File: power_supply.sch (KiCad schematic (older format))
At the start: 29 parts, among them J5 USB_A_stacked, U3 AP22802A, U4 IP4220CZ6, U5 AP2210-3.3, U8 TPS2513, U9 AP6502

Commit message: Several improvements (v0.4) after first tests
- Ultra-low-power MCU STM32L072
- Larger screw terminals
- USB power supply replaced by more efficient SMPS
- High-side load switch with P-MOS
- High-side current measurement to include USB current in load measurement
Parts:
- removed C41: 100n, LibreSolar:C_0603_1608, symbol Project:C
- removed D2: SS14FL, LibreSolar:D_SOD-123, symbol Project:D_Schottky
- removed R33, R34: 0R, LibreSolar:R_0603_1608, symbol Project:R
- removed R35: 6.8k, LibreSolar:R_0603_1608, symbol Project:R
- removed R50: 100k, LibreSolar:R_0603_1608, symbol Project:R
- removed U3: AP22802A, Package_TO_SOT_SMD:SOT-23-5, symbol Project:AP22802A
- added C2: 150u, Capacitor_SMD:CP_Elec_8x6.2, symbol Project:CP
- added C22: 2.2u, LibreSolar:C_0603_1608, symbol Project:C
- added C40: 22u, LibreSolar:C_1206_3216, symbol Project:C
- added D7: 1N4148, LibreSolar:D_SOD-123, symbol Project:D
- added D8: 11V, LibreSolar:D_SOD-123, symbol Project:D_Zener
- added J7: PWR_5V, Connector_PinHeader_2.54mm:PinHeader_1x02_P2.54mm_Vertical, symbol Connector:Conn_01x02_Male
- added Q5: BSS138N, LibreSolar:SOT-23, symbol Device:Q_NMOS_GSD
- added Q6: DMP3099L-7, LibreSolar:SOT-23, symbol Device:Q_PMOS_GSD
- added R12: 100k, LibreSolar:R_0603_1608, symbol Project:R
- added R31: 10k, LibreSolar:R_0603_1608, symbol Project:R
- added R32: 4.7, LibreSolar:R_0805_2012, symbol Project:R
- added TP7, TP8, TP9: Test_Point_Probe, TestPoint:TestPoint_Pad_D1.0mm, symbol Connector:TestPoint_Probe
- C15: value 22u -> 10u; footprint LibreSolar:C_0805_2012 -> LibreSolar:C_1210_3225; Manufacturer Murata -> Samsung; PartNumber GRM21BR61E226ME44L -> CL31A106KAHNNNE; Remarks 25V, X5R -> 25V, X7R
- C20, C21: value 47u -> 22u; footprint LibreSolar:C_0805_2012 -> LibreSolar:C_1206_3216; Manufacturer Murata -> Samsung; PartNumber GRM21BR61A476ME15K -> CL31B226MPHNNNE
- C24, U8: Config (none) -> +fastusb; DNF (none) -> X
- C29: value 1u -> 220n; footprint LibreSolar:C_0805_2012 -> LibreSolar:C_0603_1608; Manufacturer Yageo -> Murata; PartNumber CC0805KKX7R9BB105 -> GCM188R71E224KA55D; Remarks (none) -> 25V, X7R
- C36: value 6.8n -> 22u; footprint LibreSolar:C_0603_1608 -> LibreSolar:C_1206_3216; Manufacturer Yageo -> Samsung; PartNumber CC0603KRX7R9BB682 -> CL31B226MPHNNNE; Remarks (none) -> 10V
- L2: footprint Inductor_SMD:L_0805_2012Metric -> Inductor_SMD:L_1210_3225Metric; Manufacturer Murata -> Tayo Yuden; PartNumber DFE201210U-2R2M=P2 -> BRL3225T2R2M
- L3: footprint LibreSolar:Bourns_SRN6045TA -> LibreSolar:Bourns_SRN8040TA; Alternative Bourns SRN6045TA-100M -> Bourns SRN8040TA-100M; PartNumber NR6045T100M -> NR8040T100M
- R28: value 45.3k -> 100k; PartNumber RC0603FR-0745K3L -> RC0603FR-07100KL
- R29: value 10k -> 24.9k; PartNumber RC0603FR-0710KL -> RC0603FR-0724K9L
- U9: value AP6502 -> LMR33630; symbol Project:MP2307 -> LibreSolar:LMR33630; Alternatives MP2307DN-LF-Z -> (none); Manufacturer Diodes Inc. -> Texas Instruments; PartNumber AP6502ASP-13 -> LMR33630ADDA; Remarks (none) -> 400 kHz version
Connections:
- net +3V3: now also TP9.1
- net +5V: now also C24.1, C36.1, J5.1 (VBUS1), J5.5 (VBUS2), U4.5, U8.5 (IN), C40.1, D7.2 (A), J7.1 (Pin_1), TP7.1; no longer C23.1, C29.1, U5.1 (IN), U5.3 (EN)
- net GND: now also C36.2, U9.1 (PGND), C2.2, C22.2, C40.2, D8.2 (A), J7.2 (Pin_2); no longer U9.4 (GND)
- net USB_PWR_EN: now also U9.3 (EN)
- net at C19.2, L3.1: now also U9.8 (SW); no longer U9.3 (SW)
- net at C19.1: now also U9.7 (BOOT); no longer U9.1 (BS)
- net at C15.1, L2.2, U9.2 (VIN): now also C29.1, C2.1
- net at U9.6 (VCC): now also C26.1; no longer C36.1
- net +12V renamed LOAD_S
- new net: C23.1, D7.1 (K), Q6.3 (D), U5.1 (IN), U5.3 (EN)
- new net: D8.1 (K), Q5.1 (G), R31.1
- new net +10V: C22.1, Q5.2 (S), Q6.2 (S), R12.2, R32.2, TP8.1
- new net DCDC_OUT: Q5.3 (D), R31.2, R32.1
- new net PG_5V: Q6.1 (G), R12.1, U9.4 (PG)
- no-connect marks 0 -> 2
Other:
- note added: "Fast charging only on top USB port\nBottom USB port for data connection"
- note added: "Stuffing options for MOSFET\ndriver supply voltage:\n\n1. Direct supply via 12V (put R32)\n\n2. Source follower to generate\n10V from higher bat. voltage"
- note added: "Supply from 10V rail\nonly if 5V supply is \nnot good enough\n\n(maybe the gate\ncould be tied to\n5V for SMPS w/o PG)"
- note added: "Test results TP8 using 11V zener:\n- 9.28 V with MOSFET driver on \n (50 kHz)\n- 9.62 V with MOSFET driver off\n\n--> 12V zener might be better"
- note removed: "Alternative parts:\nMonolithic Power MP2307\nTI TPS5433x\nDiodes Inc. AP6502"
- moved on the sheet: C14, C15, C19, C20, C21, C23, C24, C25, C26, C35, C38, J5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

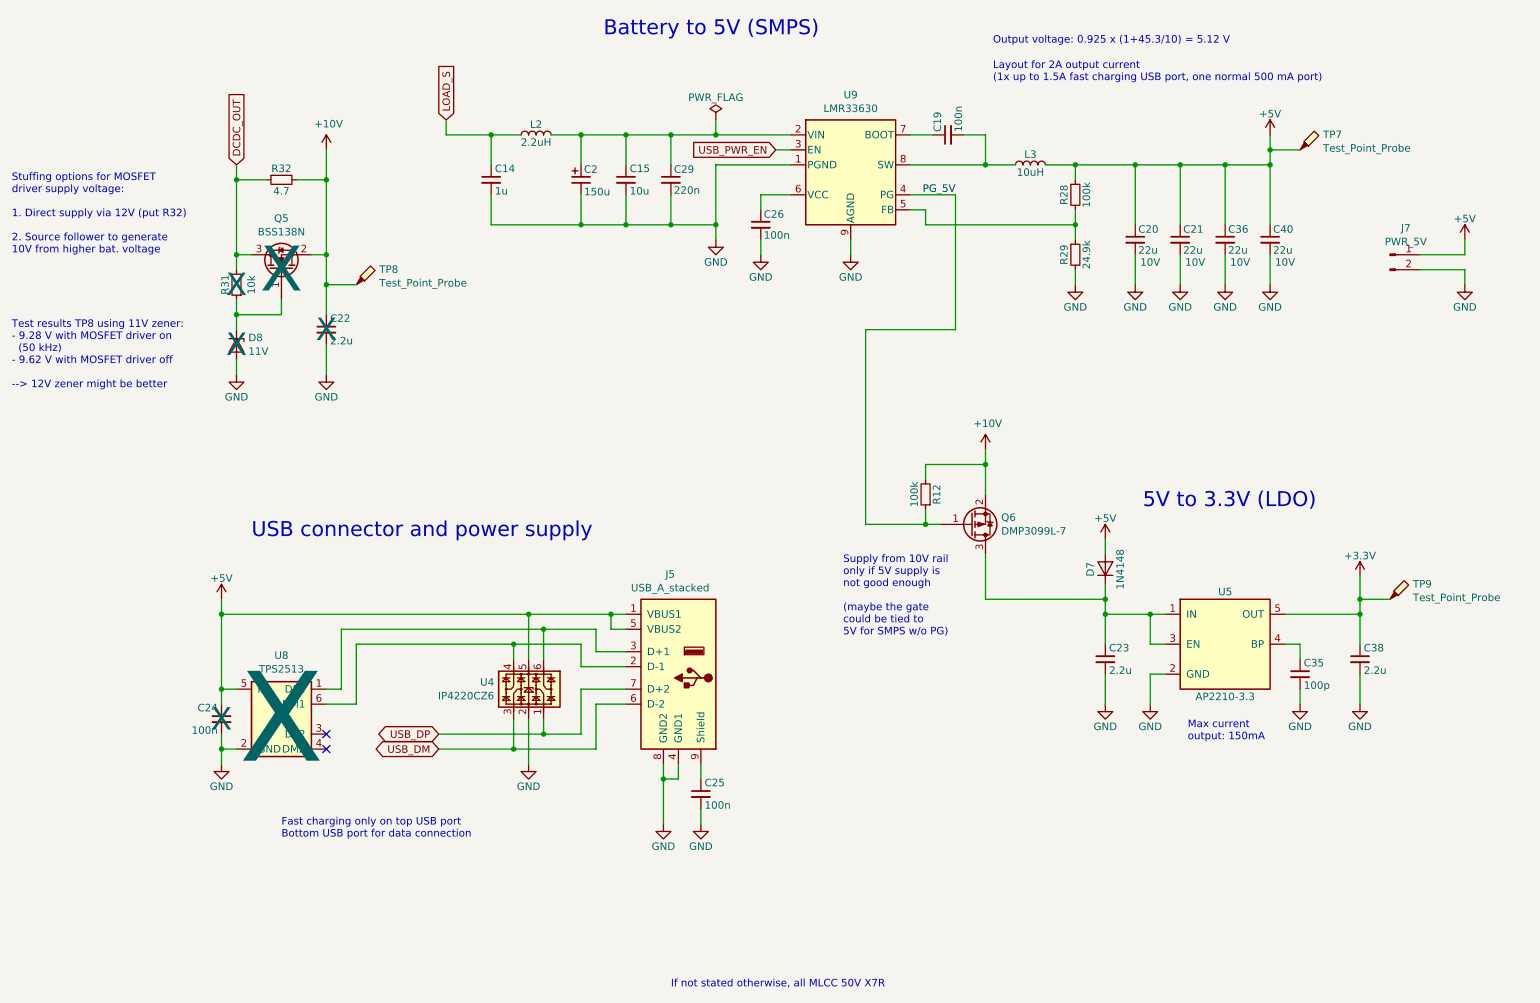
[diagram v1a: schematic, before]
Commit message: Board shape adjusted and 6P6C connector added
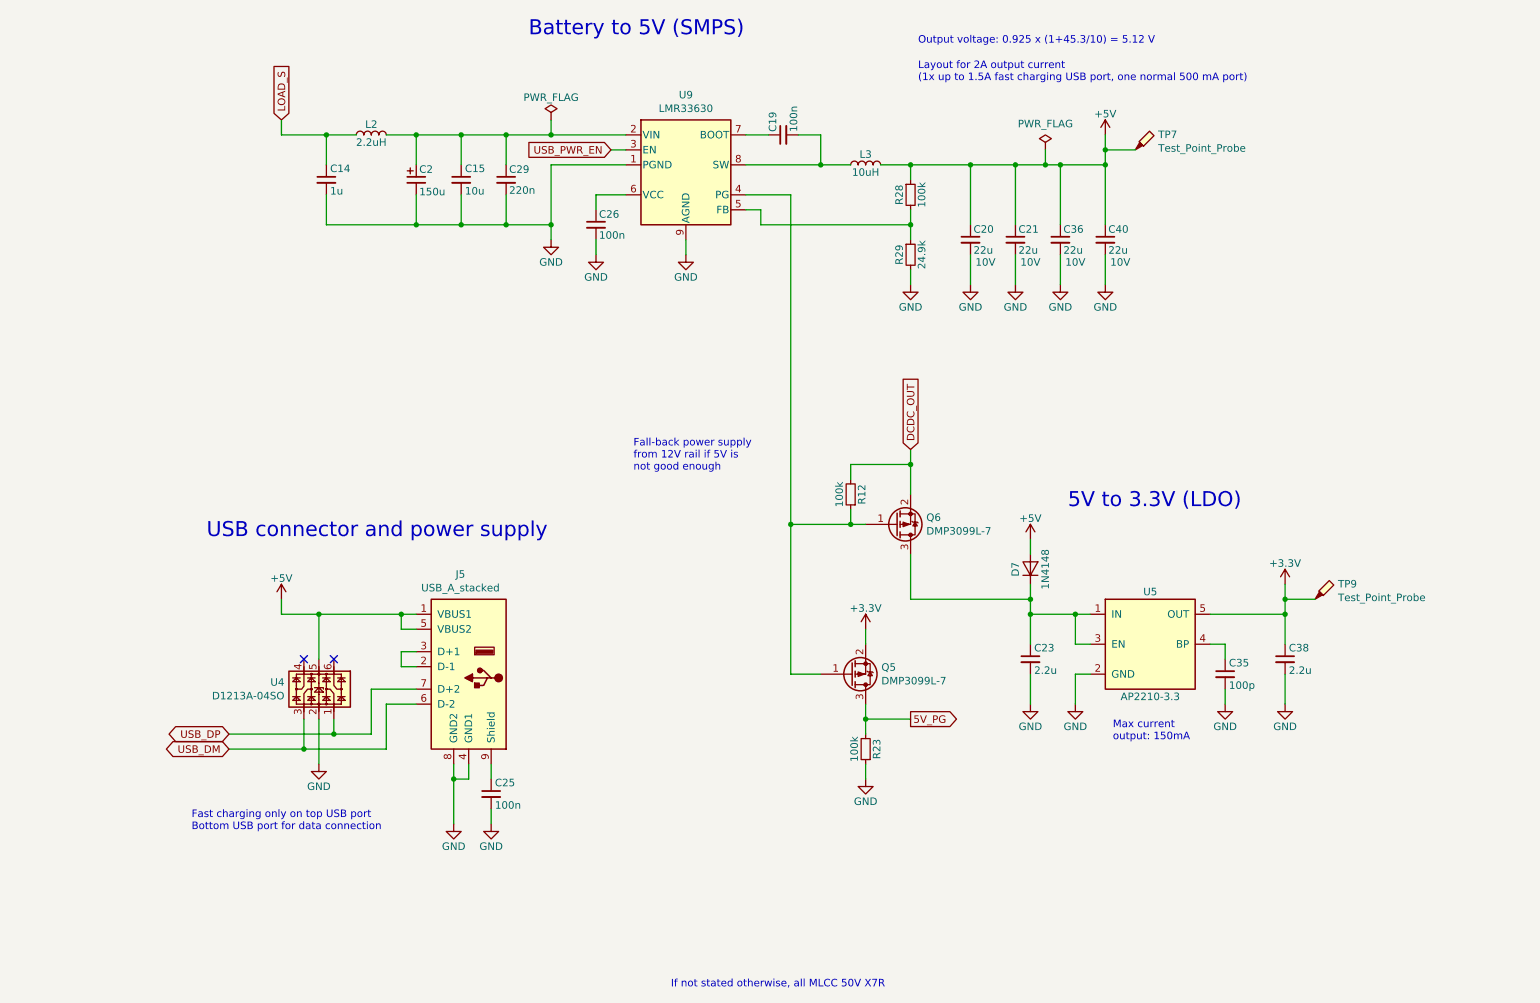
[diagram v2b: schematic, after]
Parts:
- removed C22: 2.2u, LibreSolar:C_0603_1608, symbol Project:C
- removed C24: 100n, LibreSolar:C_0603_1608, symbol Project:C
- removed D8: 11V, LibreSolar:D_SOD-123, symbol Project:D_Zener
- removed J7: PWR_5V, Connector_PinHeader_2.54mm:PinHeader_1x02_P2.54mm_Vertical, symbol Connector:Conn_01x02_Male
- removed Q5: BSS138N, LibreSolar:SOT-23, symbol Device:Q_NMOS_GSD
- removed R31: 10k, LibreSolar:R_0603_1608, symbol Project:R
- removed R32: 4.7, LibreSolar:R_0805_2012, symbol Project:R
- removed TP8: Test_Point_Probe, TestPoint:TestPoint_Pad_D1.0mm, symbol Connector:TestPoint_Probe
- removed U8: TPS2513, LibreSolar:SOT-23-6, symbol Interface_USB:TPS2513
- added Q5: DMP3099L-7, LibreSolar:SOT-23, symbol Device:Q_PMOS_GSD
- added R23: 100k, LibreSolar:R_0603_1608, symbol Project:R
- J5: Alternative Wuerth 61400826021 -> (none); Remarks (none) -> Alternative: Wuerth 61400826021
- L3: Alternative Bourns SRN8040TA-100M -> (none); Remarks (none) -> Alternative: Bourns SRN8040TA-100M
- U4: value IP4220CZ6 -> D1213A-04SO; Alternative NUP4202 -> (none); Manufacturer Nexperia -> Diodes Inc.; PartNumber IP4220CZ6 -> D1213A-04SO; Remarks (none) -> Alternative: IP4220CZ6
- U5: Alternative MIC5225 -> (none); Remarks (none) -> Alternative: MIC5225
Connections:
- net +10V is gone; now on net DCDC_OUT: Q6.2 (S), R12.2
- net +3V3: now also Q5.2 (S)
- net GND: now also R23.1
- net at J5.3 (D+1): now also J5.2 (D-1); no longer U4.6
- net at U4.4: no longer J5.2 (D-1)
- net PG_5V: no longer names the net of Q6.1 (G), R12.1, U9.4 (PG)
- net PG_5V: now also Q5.1 (G)
- new net 5V_PG: Q5.3 (D), R23.2
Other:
- note added: "Fall-back power supply \nfrom 12V rail if 5V is \nnot good enough"
- note removed: "Stuffing options for MOSFET\ndriver supply voltage:\n\n1. Direct supply via 12V (put R32)\n\n2. Source follower to generate\n10V from higher bat. voltage"
- note removed: "Supply from 10V rail\nonly if 5V supply is \nnot good enough\n\n(maybe the gate\ncould be tied to\n5V for SMPS w/o PG)"
- note removed: "Test results TP8 using 11V zener:\n- 9.28 V with MOSFET driver on \n (50 kHz)\n- 9.62 V with MOSFET driver off\n\n--> 12V zener might be better"
- moved on the sheet: C14, C15, C19, C2, C20, C21, C23, C25, C26, C29, C35, C36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

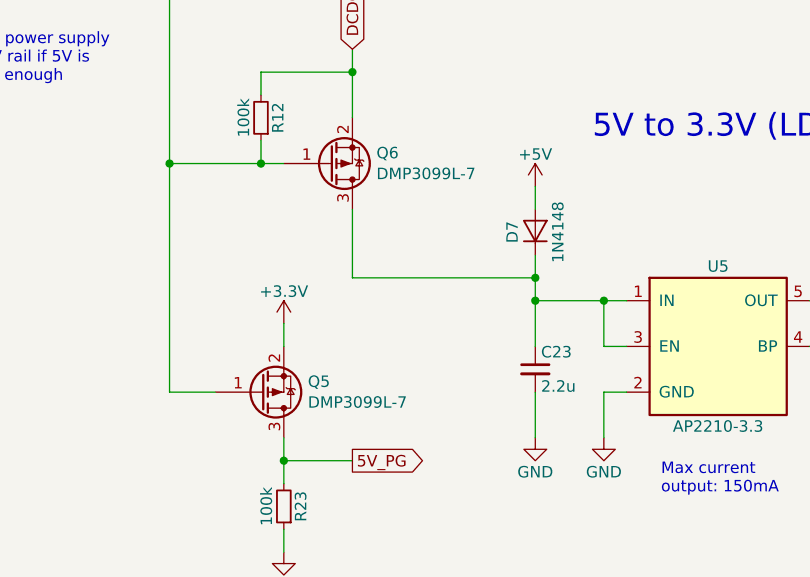
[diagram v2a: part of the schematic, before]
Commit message: Solar voltage input protection added
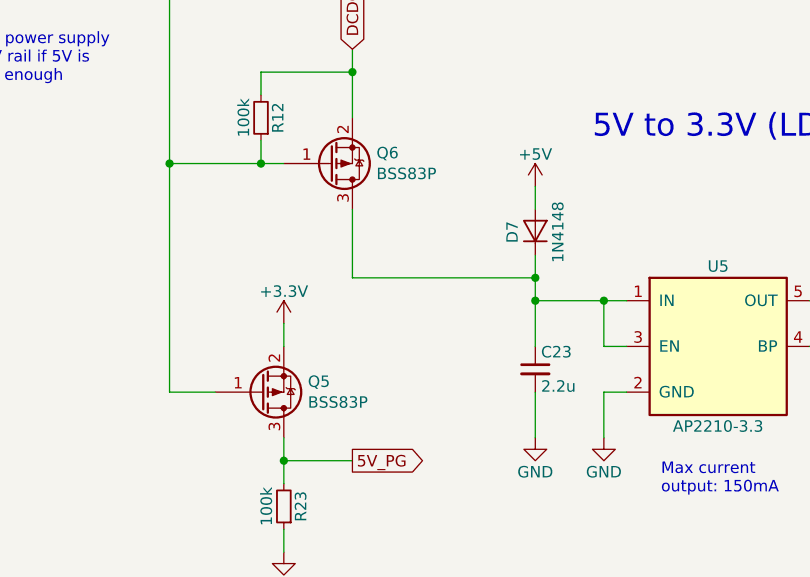
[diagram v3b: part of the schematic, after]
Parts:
- Q5, Q6: value DMP3099L-7 -> BSS83P; Manufacturer Diodes Inc. -> Infineon; PartNumber DMP3099L-7 -> BSS83P H6327; Remarks Higher current than standard BSS84 needed -> (none)
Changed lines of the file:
@@
 EESchema Schematic File Version 4
-LIBS:mptt-10a-cache
+LIBS:mppt-10a-cache
 EELAYER 29 0
 EELAYER END
@@
 Sheet 4 4
 Title "10A MPPT Charge Controller with USB"
-Date "2019-03-24"
-Rev "0.5"
+Date "2019-04-09"
+Rev "0.6"
 Comp "Libre Solar / Connected Energy"
 Comment1 "Author: Martin Jäger"
@@
 P 6600 4500
 F 0 "Q6" H 6805 4454 50  0000 L CNN
-F 1 "DMP3099L-7" H 6805 4545 50  0000 L CNN
+F 1 "BSS83P" H 6805 4545 50  0000 L CNN
 F 2 "LibreSolar:SOT-23" H 6800 4600 50  0001 C CNN
 F 3 "~" H 6600 4500 50  0001 C CNN
-F 4 "Diodes Inc." H 6600 4500 50  0001 C CNN "Manufacturer"
-F 5 "DMP3099L-7" H 6600 4500 50  0001 C CNN "PartNumber"
-F 6 "Higher current than standard BSS84 needed" H 6600 4500 50  0001 C CNN "Remarks"
+F 4 "Infineon" H 6600 4500 50  0001 C CNN "Manufacturer"
+F 5 "BSS83P H6327" H 6600 4500 50  0001 C CNN "PartNumber"
 	1    6600 4500
 	1    0    0    1
@@
 P 6300 5500
 F 0 "Q5" H 6505 5454 50  0000 L CNN
-F 1 "DMP3099L-7" H 6505 5545 50  0000 L CNN
+F 1 "BSS83P" H 6505 5545 50  0000 L CNN
 F 2 "LibreSolar:SOT-23" H 6500 5600 50  0001 C CNN
 F 3 "~" H 6300 5500 50  0001 C CNN
-F 4 "Diodes Inc." H 6300 5500 50  0001 C CNN "Manufacturer"
-F 5 "DMP3099L-7" H 6300 5500 50  0001 C CNN "PartNumber"
-F 6 "Higher current than standard BSS84 needed" H 6300 5500 50  0001 C CNN "Remarks"
+F 4 "Infineon" H 6300 5500 50  0001 C CNN "Manufacturer"
+F 5 "BSS83P H6327" H 6300 5500 50  0001 C CNN "PartNumber"
 	1    6300 5500
 	1    0    0    1
